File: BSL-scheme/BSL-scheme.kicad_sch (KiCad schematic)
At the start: 8 parts, among them J1 USB-C, Q1 Q_PMOS, U1 PIR_Sensor

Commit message: fix scheme
Подобрал делитель напряжения
Подобрал транзистор
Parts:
- removed Q1: Q_PMOS, symbol Device:Q_PMOS
- added R3: 10, Resistor_THT:R_Axial_DIN0207_L6.3mm_D2.5mm_P10.16mm_Horizontal, symbol SL_Resistors:Resistor
- added VT1: IRLML0060, DIPOS_Package_SO:SOT-23-3, symbol DIPOS_Transistor:smd-транзистор*n-канальный*2.7А*60В*sot-23*импорт
- R1: value 13k -> 6.8k
- R2: value 18k -> 4.7k
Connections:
- net 12V: now also VT1.2 (Source)
- net at LED1.2: now also VT1.3 (Drain)
- net at A1.16 (10/PWM): now also R3.2
- new net: R3.1, VT1.1 (Gate)
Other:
- moved on the sheet: LED1
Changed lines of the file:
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@@
 	(wire
 		(pts
-			(xy 183.515 63.5) (xy 208.28 63.5)
+			(xy 183.515 63.5) (xy 223.52 63.5)
 		)
 		(stroke
@@
 	(wire
 		(pts
-			(xy 208.28 91.44) (xy 208.28 100.33)
+			(xy 223.52 110.49) (xy 223.52 130.81)
 		)
 		(stroke
@@
 	(wire
 		(pts
+			(xy 223.52 82.55) (xy 223.52 90.17)
+		)
+		(stroke
+			(width 0)
+			(type default)
+		)
+	)
+	(wire
+		(pts
 			(xy 152.4 95.25) (xy 154.94 95.25)
 		)
@@
 	(wire
 		(pts
+			(xy 191.77 105.41) (xy 199.39 105.41)
+		)
+		(stroke
+			(width 0)
+			(type default)
+		)
+	)
+	(wire
+		(pts
 			(xy 183.515 63.5) (xy 183.515 71.12)
 		)
@@
 	(wire
 		(pts
-			(xy 179.705 130.81) (xy 208.28 130.81)
+			(xy 179.705 130.81) (xy 223.52 130.81)
 		)
 		(stroke
@@
 	(wire
 		(pts
-			(xy 208.28 63.5) (xy 208.28 81.28)
+			(xy 223.52 63.5) (xy 223.52 72.39)
 		)
 		(stroke
@@
 	(wire
 		(pts
+			(xy 207.01 105.41) (xy 210.82 105.41)
+		)
+		(stroke
+			(width 0)
+			(type default)
+		)
+	)
+	(wire
+		(pts
 			(xy 174.625 125.73) (xy 174.625 130.81)
 		)
@@
 	(wire
 		(pts
-			(xy 191.77 105.41) (xy 200.66 105.41)
-		)
-		(stroke
-			(width 0)
-			(type default)
-		)
-	)
-	(wire
-		(pts
 			(xy 58.42 97.79) (xy 55.88 97.79)
-		)
-		(stroke
-			(width 0)
-			(type default)
-		)
-	)
-	(wire
-		(pts
-			(xy 208.28 110.49) (xy 208.28 130.81)
 		)
 		(stroke
@@
 	)
 	(symbol
+		(lib_id "DIPOS_Transistor:smd-транзистор*n-канальный*2.7А*60В*sot-23*импорт")
+		(at 220.98 100.33 0)
+		(unit 1)
+		(exclude_from_sim no)
+		(in_bom yes)
+		(on_board yes)
+		(dnp no)
+		(fields_autoplaced yes)
+		(property "Reference" "VT1"
+			(at 231.14 97.79 0)
+			(effects
+				(font
+					(size 2.5 2.5)
+				)
+				(justify left)
+			)
+		)
+		(property "Value" "IRLML0060"
+			(at 220.98 113.03 0)
+			(effects
+				(font
+					(size 1.27 1.27)
+				)
+				(hide yes)
+			)
+		)
+		(property "Footprint" "DIPOS_Package_SO:SOT-23-3"
+			(at 220.98 118.11 0)
+			(effects
+				(font
+					(size 1.27 1.27)
+				)
+				(hide yes)
+			)
+		)
+		(property "Datasheet" "${DIPOS_DOCUMENTATION_DIR}/Транзисторы/IRLML0060TRPBF.pdf"
+			(at 220.98 115.57 0)
+			(effects
+				(font
+					(size 1.27 1.27)
+				)
+				(hide yes)
+			)
+		)
+		(property "Description" "Транзистор N-канальный маленький силовой"
+			(at 220.98 100.33 0)
+			(effects
+				(font
+					(size 1.27 1.27)
+				)
+				(hide yes)
+			)
+		)
+		(property "INFO" "2,7A 60В"
+			(at 231.14 102.87 0)
+			(effects
+				(font
+					(size 2.5 2.5)
+				)
+				(justify left)
+			)
+		)
+		(property "NAME" "Транзистор SOT-23 MOSFET N-канальный IRLML0060"
+			(at 220.98 120.65 0)
+			(effects
+				(font
+					(size 1.27 1.27)
+				)
+				(hide yes)
+			)
+		)
+		(pin "3"
+		)
+		(pin "1"
+		)
+		(pin "2"
+		)
+		(instances
+			(project ""
+				(path "/85e4e3d9-5ce6-4b3f-8c48-5d83bde13bc2"
+					(reference "VT1")
+					(unit 1)
+				)
+			)
+		)
+	)
+	(symbol
 		(lib_name "#метка-12V_1")
 		(lib_id "niisk_lib:#метка-12V")
@@
 	(symbol
 		(lib_id "petr_chip:smd_led_0603")
-		(at 208.28 81.28 270)
+		(at 223.52 72.39 270)
 		(unit 1)
 		(exclude_from_sim no)
@@
 		(dnp no)
 		(property "Reference" "LED1"
-			(at 201.93 81.28 90)
+			(at 217.17 72.39 90)
 			(effects
 				(font
@@
 		)
 		(property "Value" "smd_led_0603"
-			(at 203.2 86.36 0)
+			(at 218.44 77.47 0)
 			(effects
 				(font
@@
 		)
 		(property "Footprint" "MOTOR_VD_VT_HL:Светодиод_SMD_IEC_0603"
-			(at 201.168 87.122 0)
+			(at 216.408 78.232 0)
 			(effects
 				(font
@@
 		)
 		(property "Datasheet" ""
-			(at 208.28 84.709 0)
+			(at 223.52 75.819 0)
 			(effects
 				(font
@@
 		)
 		(property "Description" ""
-			(at 208.28 81.28 0)
+			(at 223.52 72.39 0)
 			(effects
 				(font
@@
 		)
 		(property "NAME" ""
-			(at 208.28 82.55 0)
+			(at 223.52 73.66 0)
 			(effects
 				(font
@@
 	)
 	(symbol
-		(lib_id "Device:Q_PMOS")
-		(at 205.74 105.41 0)
+		(lib_id "SL_Resistors:Resistor")
+		(at 203.2 105.41 180)
 		(unit 1)
 		(exclude_from_sim no)
@@
 		(dnp no)
 		(fields_autoplaced yes)
-		(property "Reference" "Q1"
-			(at 212.09 105.4099 0)
-			(effects
-				(font
-					(size 1.27 1.27)
-				)
-				(justify left)
-			)
-		)
-		(property "Value" "Q_PMOS"
-			(at 212.09 106.6799 0)
-			(effects
-				(font
-					(size 1.27 1.27)
-				)
-				(justify left)
-				(hide yes)
-			)
-		)
-		(property "Footprint" ""
-			(at 210.82 102.87 0)
-			(effects
-				(font
-					(size 1.27 1.27)
-				)
-				(hide yes)
-			)
-		)
-		(property "Datasheet" "~"
-			(at 205.74 105.41 0)
-			(effects
-				(font
-					(size 1.27 1.27)
-				)
-				(hide yes)
-			)
-		)
-		(property "Description" "P-MOSFET transistor"
-			(at 205.74 105.41 0)
-			(effects
-				(font
-					(size 1.27 1.27)
-				)
-				(hide yes)
-			)
-		)
-		(pin "G"
-		)
-		(pin "S"
-		)
-		(pin "D"
+		(property "Reference" "R3"
+			(at 203.2 99.06 0)
+			(effects
+				(font
+					(size 1.27 1.27)
+				)
+			)
+		)
+		(property "Value" "10"
+			(at 203.2 101.6 0)
+			(effects
+				(font
+					(size 1.27 1.27)
+				)
+			)
+		)
+		(property "Footprint" "Resistor_THT:R_Axial_DIN0207_L6.3mm_D2.5mm_P10.16mm_Horizontal"
+			(at 202.311 101.092 0)
+			(effects
+				(font
+					(size 1.27 1.27)
+				)
+				(hide yes)
+			)
+		)
+		(property "Datasheet" ""
+			(at 202.692 105.41 0)
+			(effects
+				(font
+					(size 1.27 1.27)
+				)
+				(hide yes)
+			)
+		)
+		(property "Description" "1/4W Resistor"
+			(at 203.2 105.41 0)
+			(effects
+				(font
+					(size 1.27 1.27)
+				)
+				(hide yes)
+			)
+		)
+		(pin "1"
+		)
+		(pin "2"
 		)
 		(instances
-			(project ""
+			(project "BSL-scheme"
 				(path "/85e4e3d9-5ce6-4b3f-8c48-5d83bde13bc2"
-					(reference "Q1")
+					(reference "R3")
 					(unit 1)
 				)
@@
 			)
 		)
-		(property "Value" "18k"
+		(property "Value" "4.7k"
 			(at 157.48 104.1399 90)
 			(effects
@@
 		(on_board yes)
 		(dnp no)
-		(fields_autoplaced yes)
 		(property "Reference" "R1"
 			(at 148.59 88.9 0)
@@
 			)
 		)
-		(property "Value" "13k"
+		(property "Value" "6.8k"
 			(at 148.59 91.44 0)
 			(effects

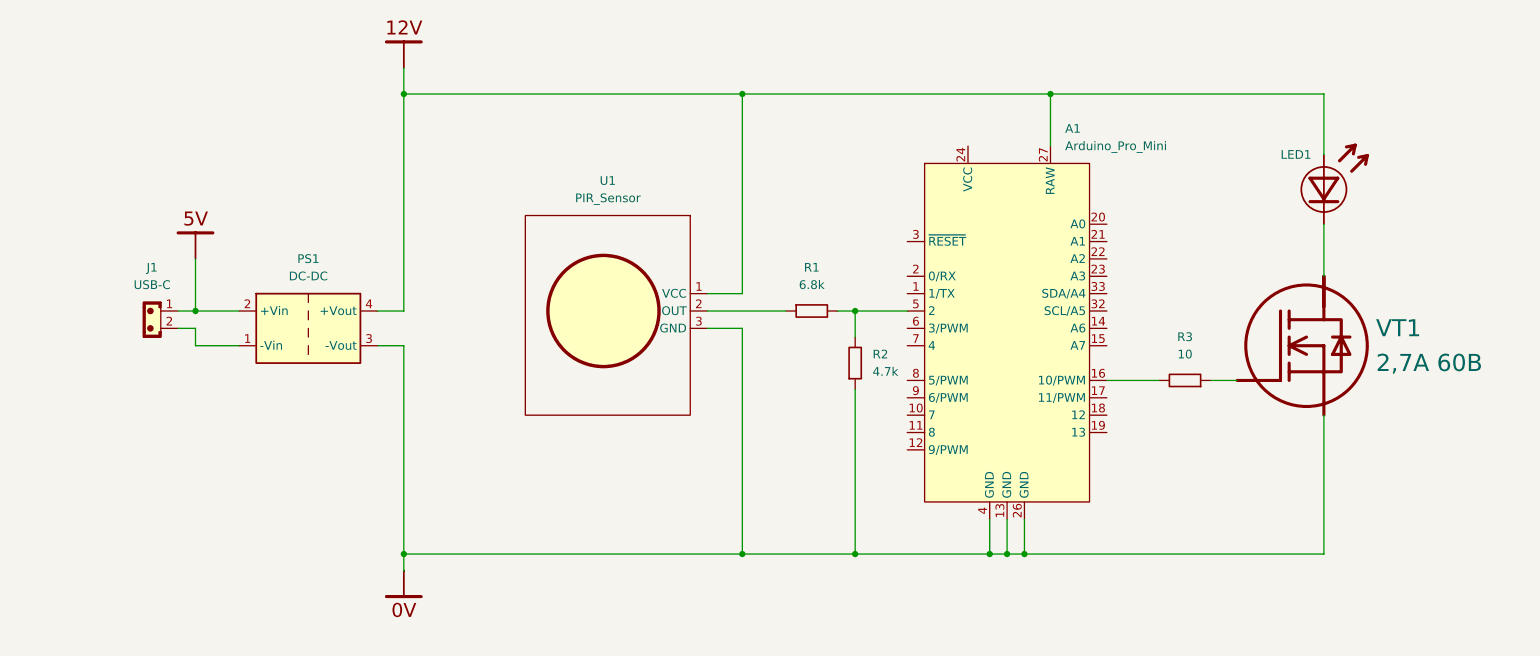
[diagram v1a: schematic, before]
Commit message: fix scheme
Разделил нули датчика движения
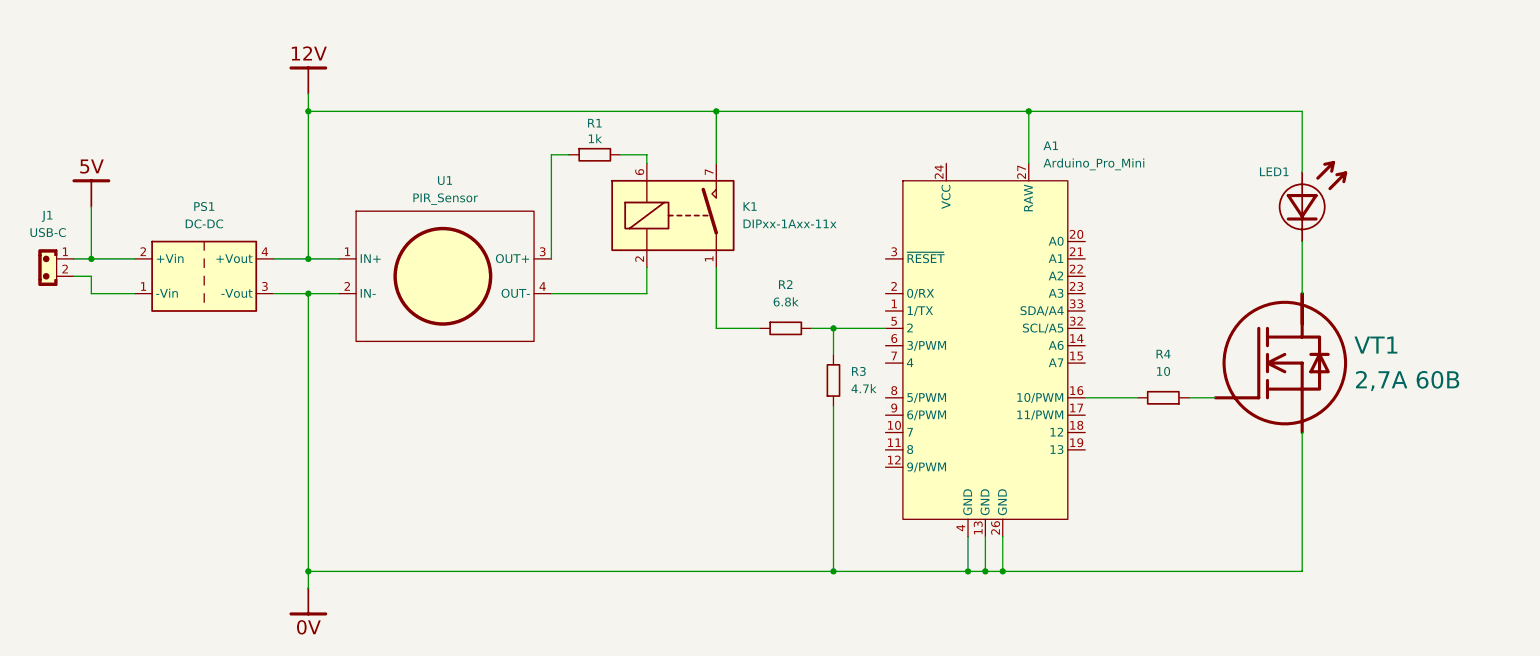
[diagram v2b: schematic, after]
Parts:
- added K1: DIPxx-1Axx-11x, Relay_THT:Relay_StandexMeder_DIP_LowProfile, symbol Relay:DIPxx-1Axx-11x
- added R1: 1k, Resistor_THT:R_Axial_DIN0207_L6.3mm_D2.5mm_P10.16mm_Horizontal, symbol SL_Resistors:Resistor
- renumbered R1 to R2, R2 to R3, R3 to R4
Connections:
- net 12V: now also U1.2 (IN-), K1.7, K1.8; no longer U1.3 (GND)
- net at R2.1: now also K1.1, K1.14; no longer U1.2 (OUT)
- new net: R1.1, U1.3 (OUT+)
- new net: K1.6, R1.2
- new net: K1.2, U1.4 (OUT-)
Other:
- moved on the sheet: A1, J1, LED1, PS1, R2, R3, R4, VT1

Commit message: scheme is work
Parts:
- removed R3: 4.7k, Resistor_THT:R_Axial_DIN0207_L6.3mm_D2.5mm_P10.16mm_Horizontal, symbol SL_Resistors:Resistor
- R1: renamed from R2; value 6.8k -> 11k
- R2: renamed from R1; value 1k -> 4.6k
- renumbered R4 to R3
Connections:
- net 12V: now also K1.14, K1.3; no longer K1.7, K1.8
- net at R2.2: now also K1.1; no longer K1.6
- net at A1.24 (VCC): now also R1.2
- net at A1.5 (2): now also K1.4, K1.8, R1.1; no longer R1.2
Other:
- moved on the sheet: A1, J1, PS1, R1, R2, U1

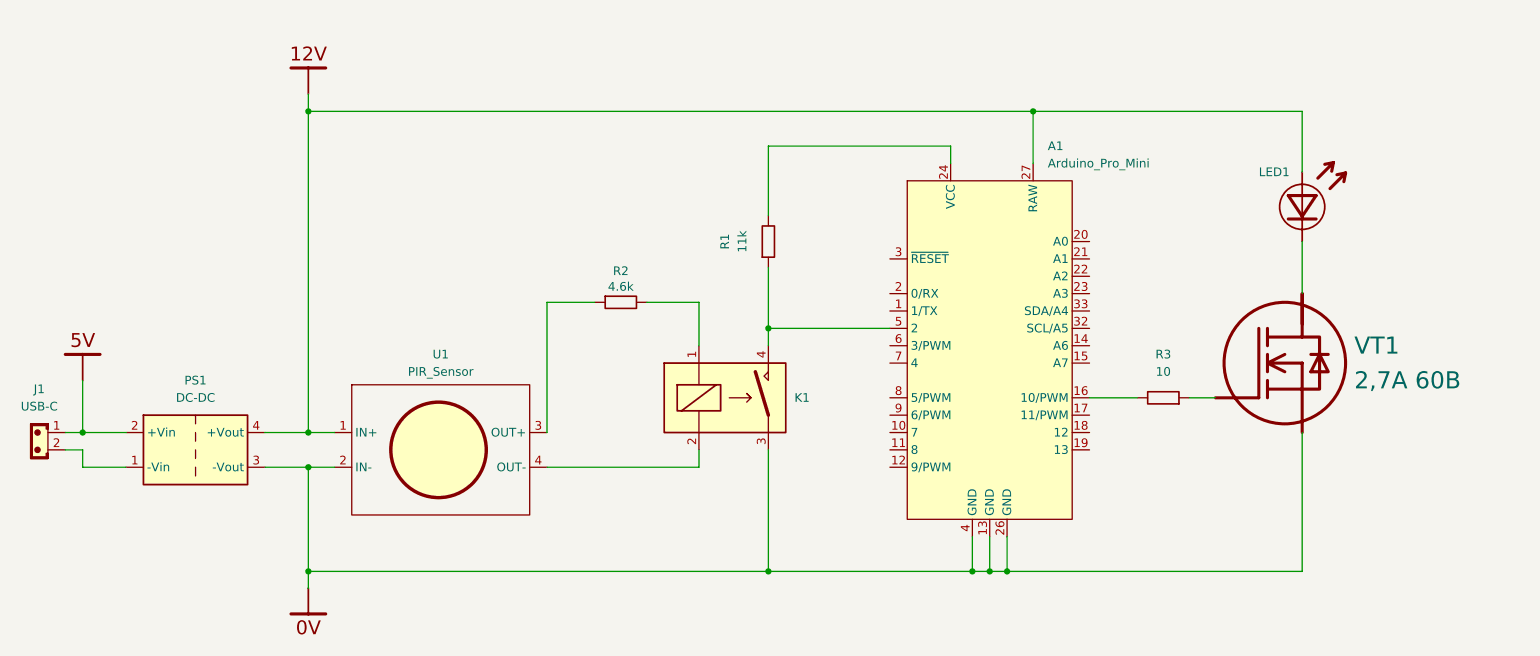
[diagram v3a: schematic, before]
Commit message: fix scheme
Поменял распиновку контроллера
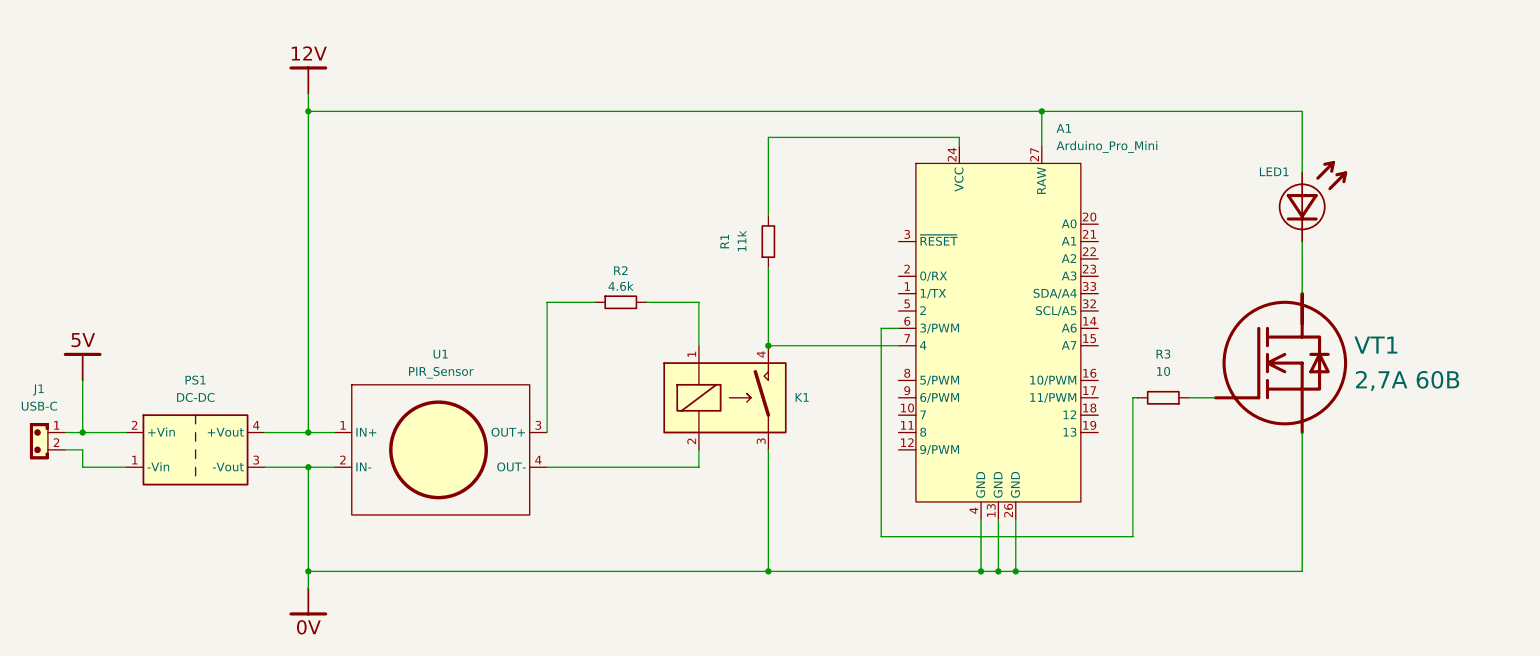
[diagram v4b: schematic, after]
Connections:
- net at K1.4, K1.8, R1.1: now also A1.7 (4); no longer A1.5 (2)
- net at A1.16 (10/PWM): no longer R3.2
- net at A1.6 (3/PWM): now also R3.2
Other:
- moved on the sheet: A1
